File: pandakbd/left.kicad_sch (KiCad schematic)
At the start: 34 parts, among them J1 Conn_ST_STDC14, SW65 MK-12C03-G015, U1 LDI1117, U2 USBLC6-2SC6_C5261088, U3 358, U4 STM32F446RCTx, U5 GT-TC020A-H035-L05, Y1 8MHz

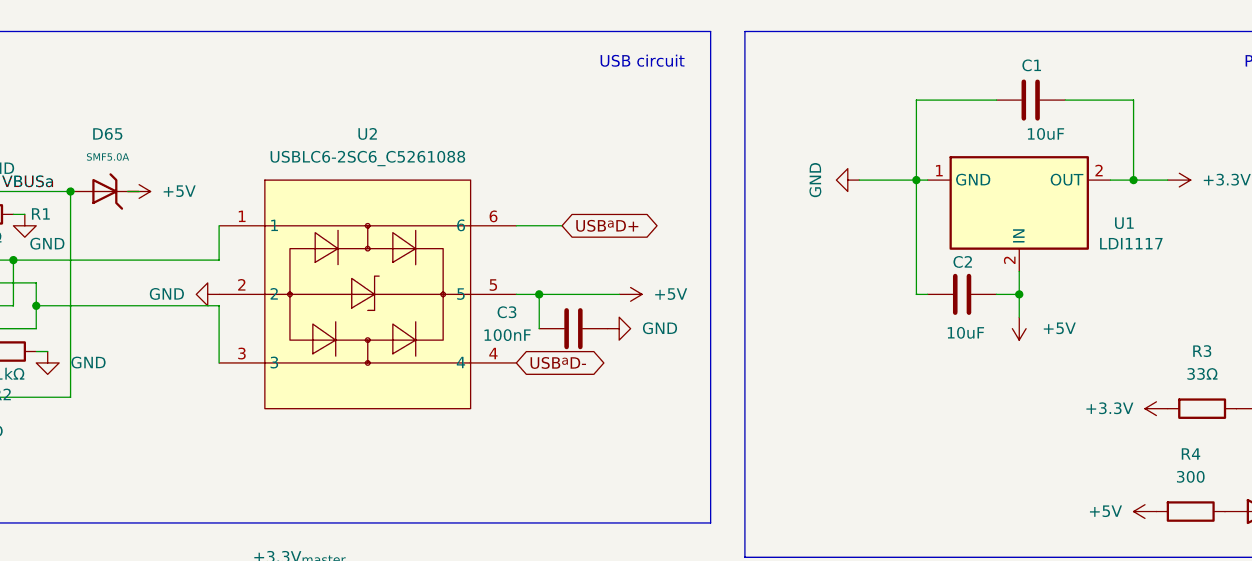
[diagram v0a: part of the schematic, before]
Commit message: prepare placing components
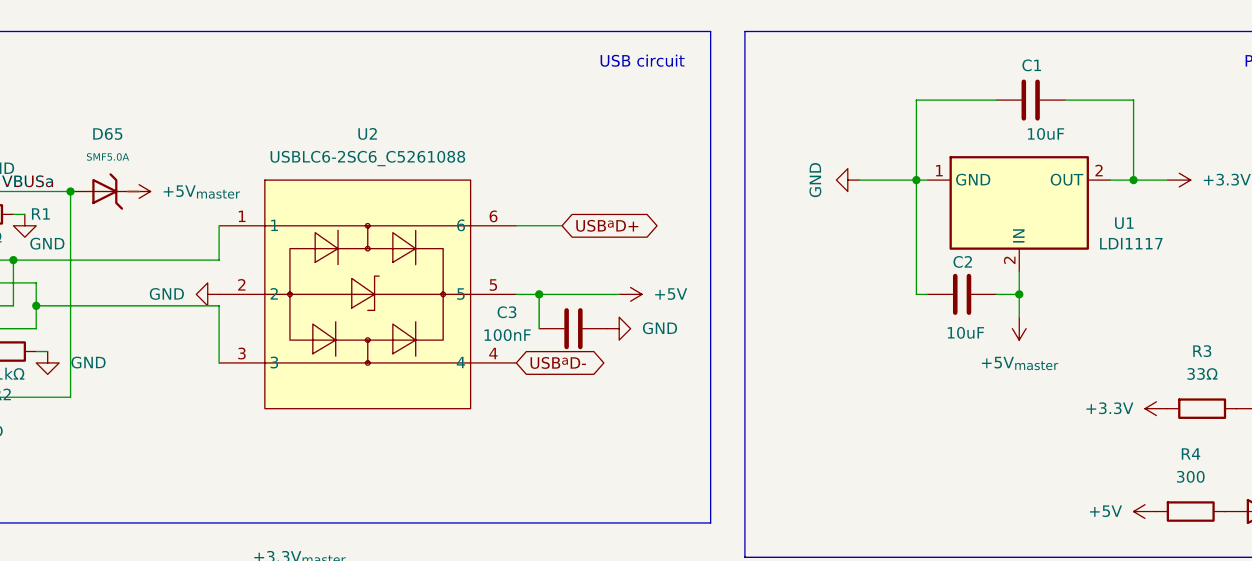
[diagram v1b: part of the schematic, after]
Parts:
- U2: footprint easyeda2kicad:SOT-23-6_L2.9-W1.6-P0.95-LS2.8-BR -> Package_TO_SOT_SMD:SOT-23-6
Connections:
- net +5V: no longer C2.2, D65.1, U1.2 (OUT)
- new net +5V_{master}: C2.2, D65.1, U1.2 (OUT)
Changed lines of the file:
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@@
 			)
 		)
-		(property "Value" "+5V"
-			(at 157.48 46.9899 0)
-			(effects
-				(font
-					(size 1.27 1.27)
-				)
-				(justify right)
+		(property "Value" "+5V_{master}"
+			(at 154.94 50.8 0)
+			(effects
+				(font
+					(size 1.27 1.27)
+				)
 			)
 		)
@@
 			)
 		)
-		(property "Value" "+5V"
+		(property "Value" "+5V_{master}"
 			(at 59.69 31.7499 90)
 			(effects
@@
 			)
 		)
-		(property "Footprint" "easyeda2kicad:SOT-23-6_L2.9-W1.6-P0.95-LS2.8-BR"
+		(property "Footprint" "Package_TO_SOT_SMD:SOT-23-6"
 			(at 82.55 58.42 0)
 			(effects
